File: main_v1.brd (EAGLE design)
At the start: 79.4 x 80.6 mm, 45 parts, among them IC1 MEGA8-P, IC2 7805TV, IC4 MC33063/MC34063P, IC5 MAX6921, IC6 MAX6921

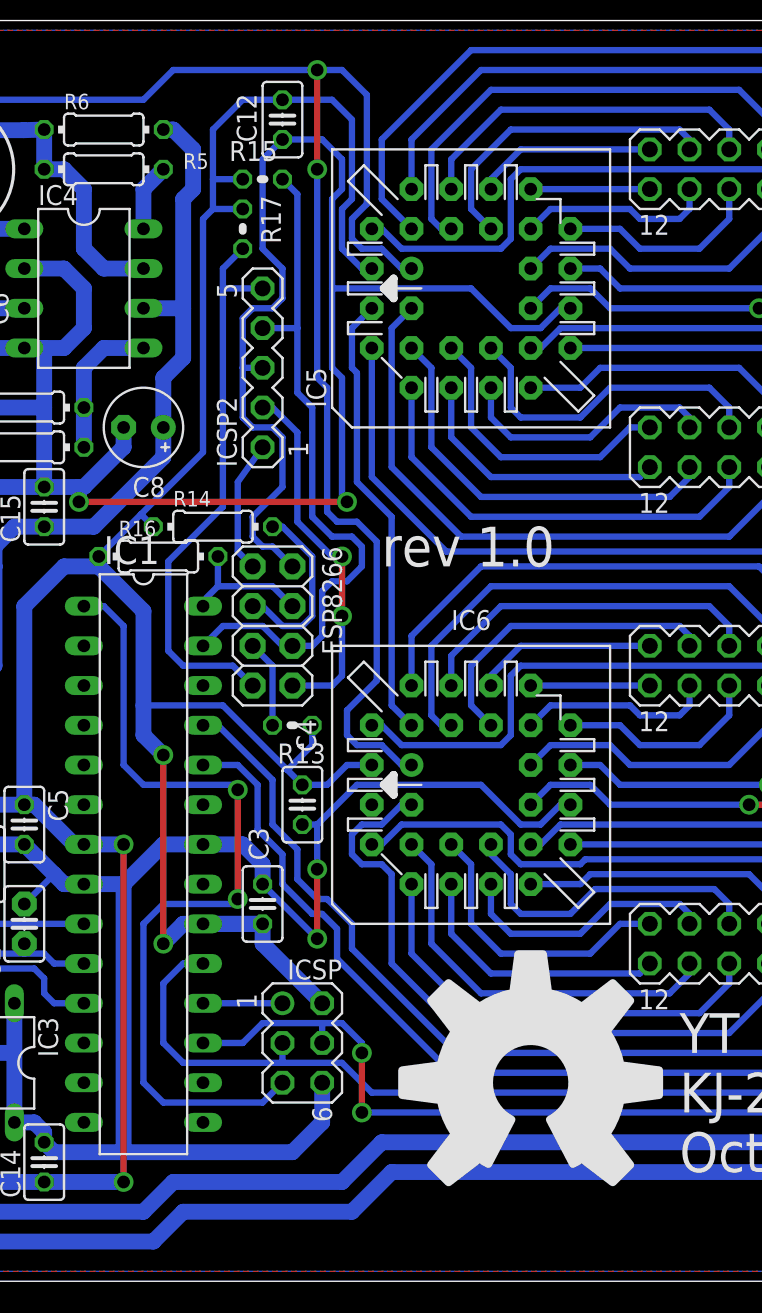
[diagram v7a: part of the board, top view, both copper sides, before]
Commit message: Fix ESP socket connections
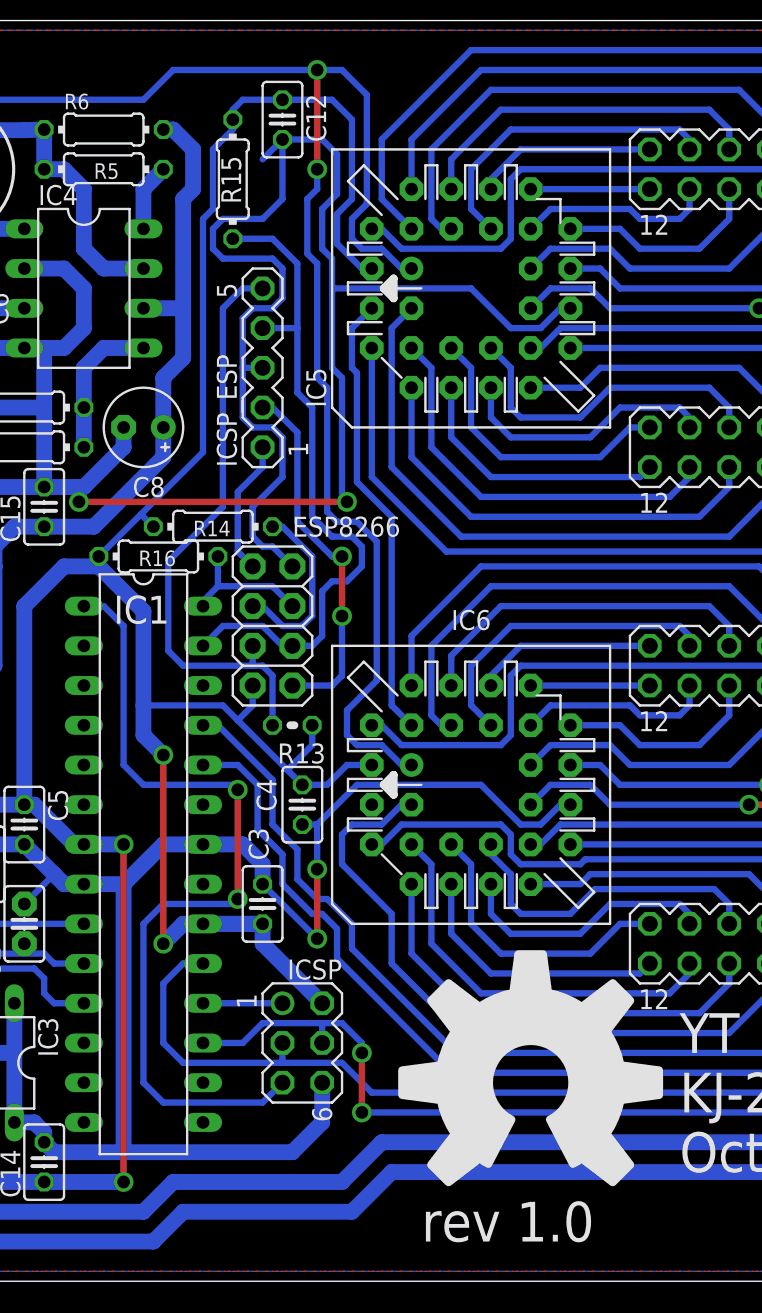
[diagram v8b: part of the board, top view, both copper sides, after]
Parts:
- removed R17: (no value), resistor:0204V
- R15: value (none) -> 4k7; device resistor:0204V -> resistor:0204/7
- R16: value (none) -> 4k7
- moved R15 1.91 mm to (31.1, 70.5), turned to 270 degrees
- renumbered ICSP2 to ICSP_ESP
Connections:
- net N$10 renamed TX
- net N$14 renamed RX
- net N$17 renamed CHPD
- removed net N$12: ESP8266.7, ICSP_ESP.5, R17.2
- removed net N$19: ESP8266.5, R13.2
- new net ESP_RST: ESP8266.5, ICSP_ESP.5, R13.2
- net VCC: now also ESP8266.7; no longer R17.1
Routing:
- net ESP_RST: track 0.00 -> 38.2 mm
- net N$12: track 36.5 -> 0.00 mm
- net GND: track 304.2 -> 312.2 mm
- net N$19: track 5.61 -> 0.00 mm
- net SDA: track 44.8 -> 43.8 mm
- net VCC: track 195.6 -> 194.7 mm
- net VBB: track 127.5 -> 128.1 mm
